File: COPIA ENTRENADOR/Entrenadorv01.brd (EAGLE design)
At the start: 116.1 x 96.2 mm, 67 parts, among them IC1 7805T, X1 MINI-USB_4P-85-32004-10X

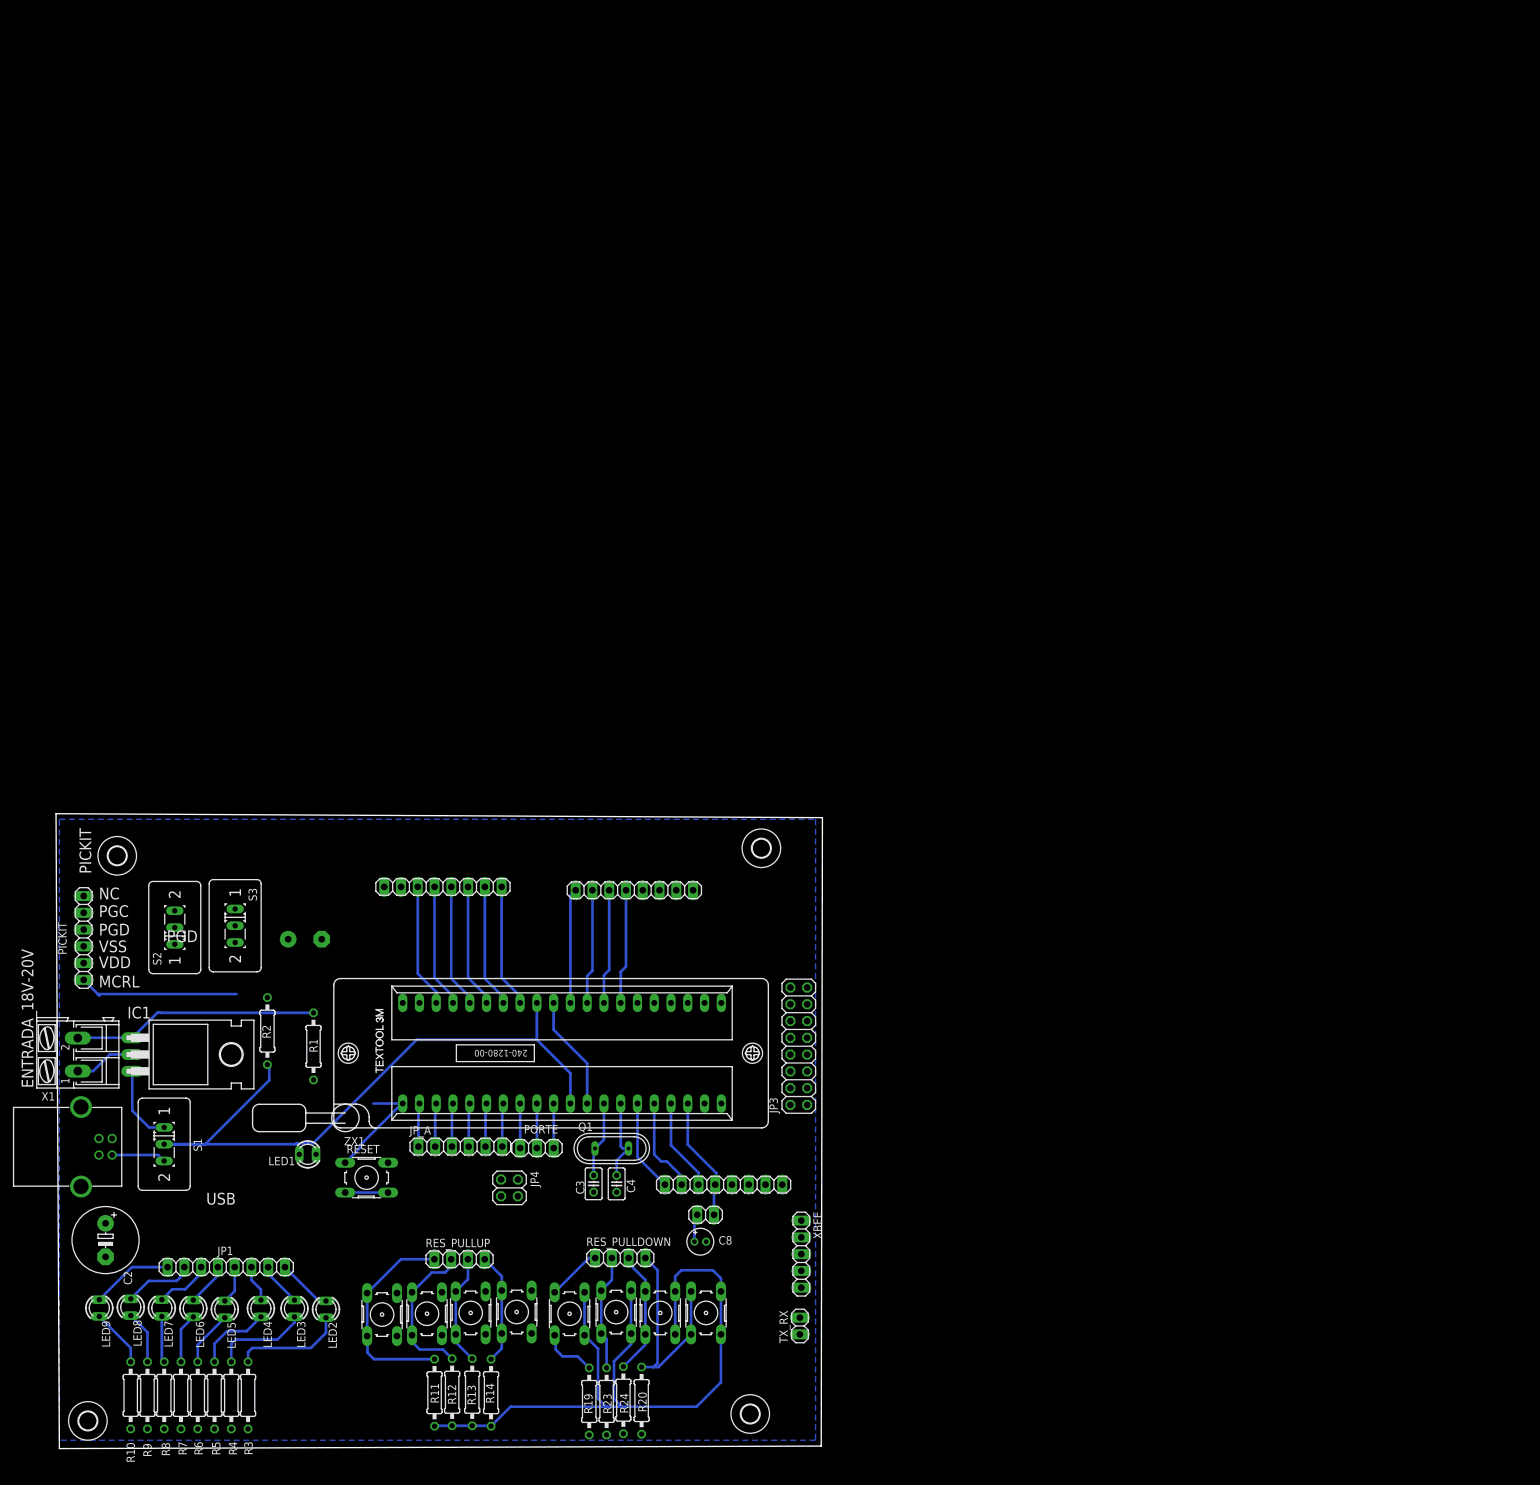
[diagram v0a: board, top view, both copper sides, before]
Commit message: se agrega diseño PCB
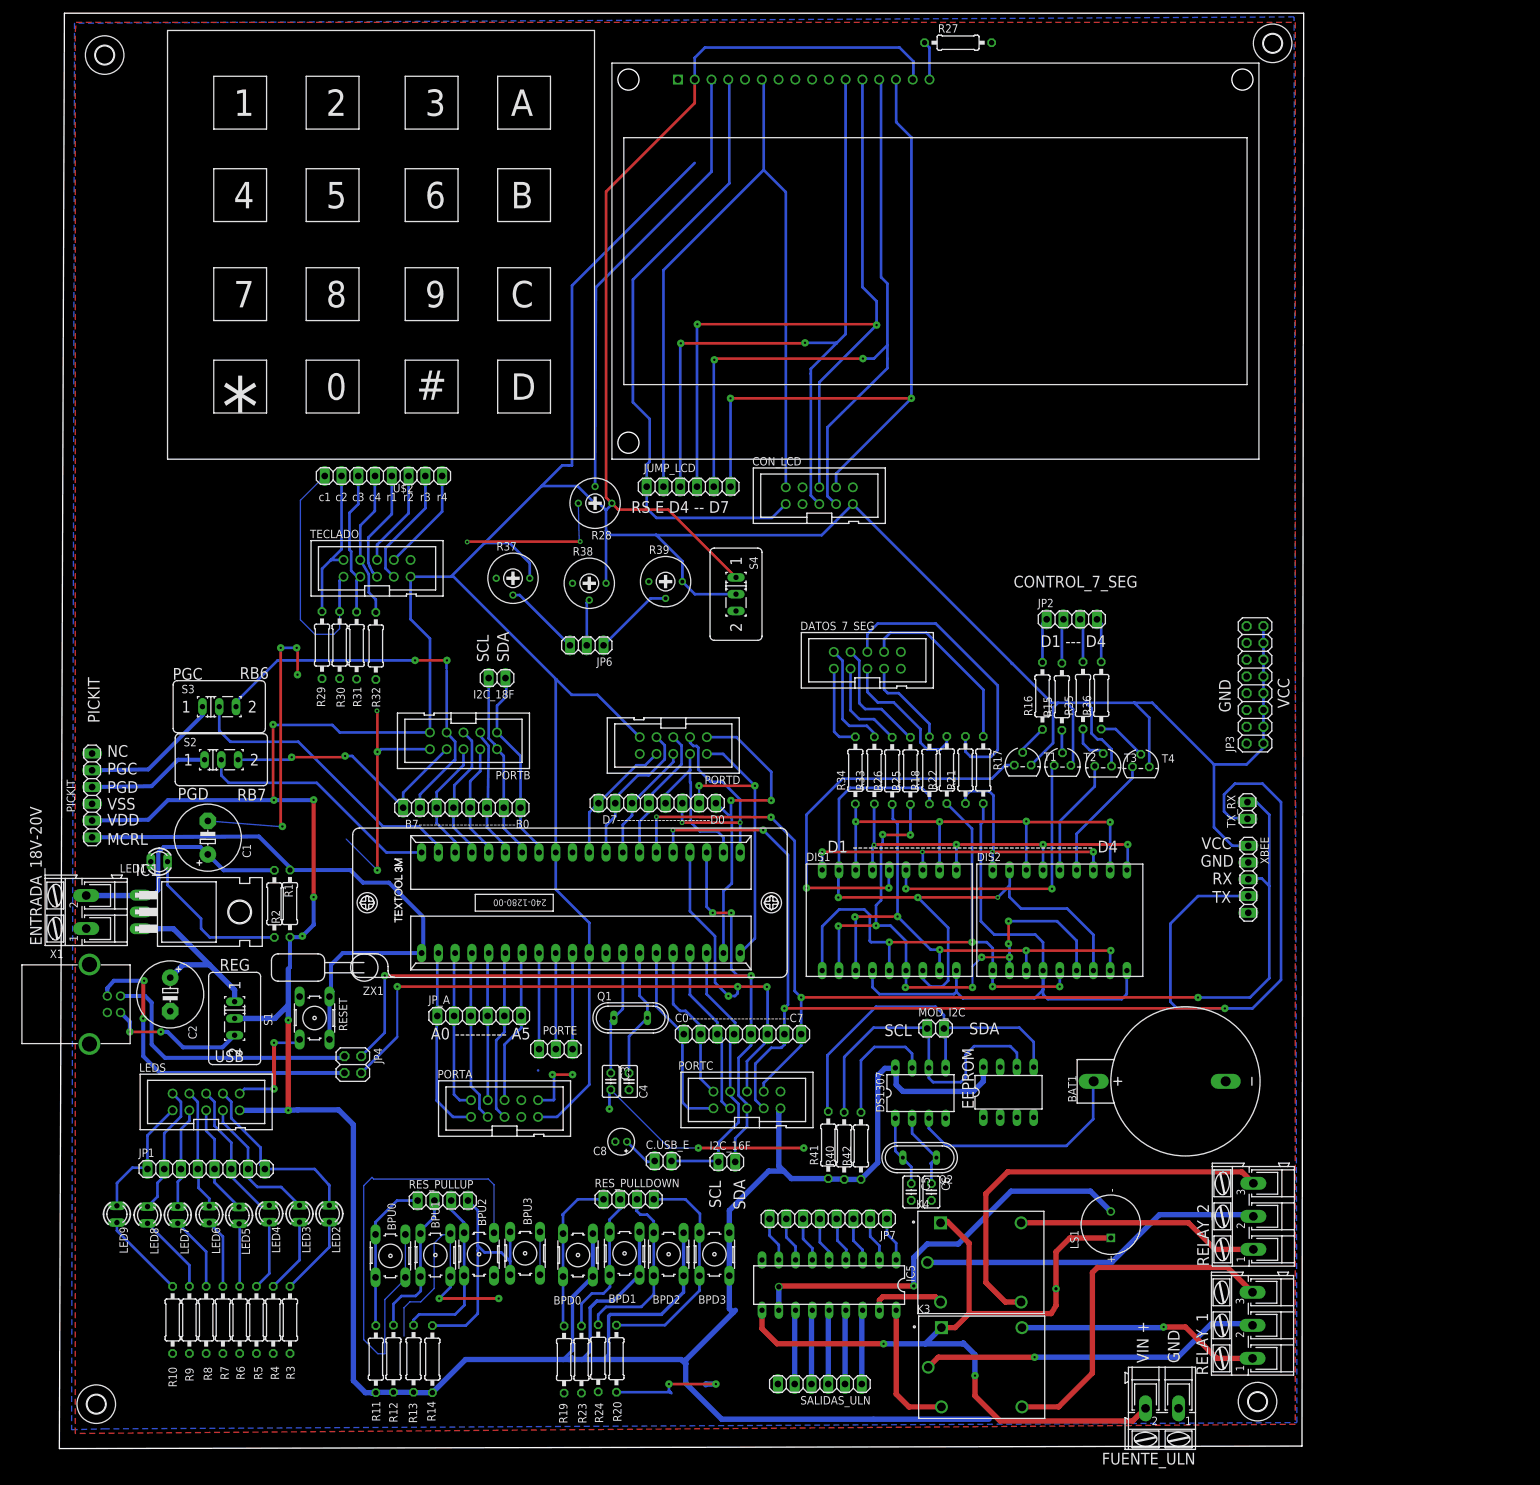
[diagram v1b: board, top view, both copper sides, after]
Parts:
- added BAT1: (no value), sn2032:SN2032
- added C5, C6: (no value), rcl:C025-025X050
- added CON_LCD, DATOS_7_SEG, LEDS, PORTA, PORTB, PORTC, PORTD, TECLADO: 2510-, con-3m:PAK100/2500-10
- added DIS1, DIS2: HD-K123, display-hp:HDSP-R
- added DS1307: DS1307, ds1307_pcf8583:DIL08
- added EEPROM: 24LC256P, microchip:DIL8
- added FUENTE_ULN: (no value), con-ptr500:AK300/2
- added I2C_16F, I2C_18F, MOD_I2C: (no value), pinhead:1X02
- added IC5: (no value), uln-udn:DIL18
- added JP2: (no value), pinhead:1X04
- added JP6: (no value), pinhead:1X03
- added JP7: (no value), pinhead:1X08
- added JUMP_LCD, SALIDAS_ULN: (no value), pinhead:1X06
- added K3, K4: SRD-05VDC-SL-C, SRD-05VDC-SL-C (1):RELAY_SRD-05VDC-SL-C
- added LS1: CST-951AP, CST-951AP:CUI_CST-951AP
- added Q2: (no value), special:QS
- added R15, R16, R29, R30, R31, R32, R35, R36: 10K, rcl:0207/10
- added R17, R18, R21, R22, R25, R26, R27, R33, R34: 330, rcl:0207/10
- added R28, R37, R38, R39: 5K, rcl:RTRIM3339P
- added R40, R41, R42: 10k, rcl:0207/10
- added RELAY_1, RELAY_2: (no value), con-ptr500:AK300/3
- added S4: (no value), switch:M251
- added T1, T2, T3, T4: 2N3904, transistor:TO92
- added U$1: LCD-HD4478020X4-3HOLES, HD44780LCD:LCD-20X4-3HOLES
- added U$2: (no value), keypad_4x4_raw:KEYPAD4X4
- moved U$6 144.4 mm to (183.8, 212.9)
- moved U$5 121.3 mm to (6.86, 211.1)
- moved TX_RX 103.4 mm to (180.0, 96.6)
- moved XBEE 88.4 mm to (180.1, 86.2)
- moved JP3 88.2 mm to (181.1, 115.7)
- moved U$4 76.9 mm to (181.5, 7.11)
- moved LED1 49.7 mm to (15.1, 88.9)
- moved C2 38.5 mm to (16.8, 68.8)
- moved S3 33.3 mm to (24.2, 112.4), turned to 0 degrees
- moved JP4 30.2 mm to (44.5, 58.2)
- moved S2 26.4 mm to (24.5, 104.3), turned to 0 degrees
- moved RESET 25.4 mm to (38.6, 65.2), turned to 270 degrees
- moved ZX1 23.0 mm to (79.0, 82.7)
- moved C0---------------------------C7 23.0 mm to (103.5, 62.8)
- moved R1 22.4 mm to (32.6, 82.5)
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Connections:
- new net A: DIS1.11, DIS1.16, DIS2.11, DIS2.16, R34.1
- new net B: DIS1.10, DIS1.15, DIS2.10, DIS2.15, R33.1
- new net C: DIS1.3, DIS1.8, DIS2.3, DIS2.8, R26.1
- new net D: DIS1.2, DIS1.6, DIS2.2, DIS2.6, R25.1
- new net E: DIS1.1, DIS1.5, DIS2.1, DIS2.5, R22.1
- new net F: DIS1.12, DIS1.18, DIS2.12, DIS2.18, R21.1
- new net G: DIS1.17, DIS1.7, DIS2.17, DIS2.7, R18.1
- new net N$10: JP6.2, R38.2
- new net N$100: FUENTE_ULN.2, IC5.10, K3.A1, K4.A1, LS1.P
- new net N$101: R28.1, S4.1, U$1.P$15, U$1.P$2
- new net N$12: JP6.3, R37.2
- new net N$13: R27.1, U$1.P$16
- new net N$14: JP6.1, R39.2
- new net N$15: IC5.1, JP7.1
- new net N$18: CON_LCD.8, JUMP_LCD.6, U$1.P$14
- new net N$19: CON_LCD.7, JUMP_LCD.5, U$1.P$13
- new net N$20: IC5.2, JP7.2
- new net N$21: CON_LCD.6, JUMP_LCD.4, U$1.P$12
- new net N$22: DS1307.6, EEPROM.6, MOD_I2C.1, R40.2
- new net N$23: CON_LCD.5, JUMP_LCD.3, U$1.P$11
- new net N$24: IC5.3, JP7.3
- new net N$25: CON_LCD.1, JUMP_LCD.1, U$1.P$4
- new net N$26: DIS1.4, DIS1.9, DIS2.4, DIS2.9, R17.2
- new net N$27: CON_LCD.2, JUMP_LCD.2, U$1.P$6
- new net N$28: R30.1, TECLADO.1, U$2.1
- new net N$29: R28.2, U$1.P$3
- new net N$30: R29.1, TECLADO.2, U$2.2
- new net N$31: R31.1, TECLADO.3, U$2.3
- new net N$32: R32.1, TECLADO.4, U$2.4
- new net N$33: TECLADO.5, U$2.5
- new net N$34: TECLADO.6, U$2.6
- new net N$35: TECLADO.7, U$2.7
- new net N$36: TECLADO.8, U$2.8
- new net N$37: DATOS_7_SEG.7, R18.2
- new net N$38: R16.1, T1.2
- new net N$40: R15.1, T2.2
- new net N$41: DIS1.13, T2.3
- new net N$42: DIS1.14, T1.3
- new net N$59: DATOS_7_SEG.6, R21.2
- new net N$60: JP2.1, R16.2
- new net N$61: JP2.2, R15.2
- new net N$62: DATOS_7_SEG.5, R22.2
- new net N$63: DATOS_7_SEG.4, R25.2
- new net N$64: DATOS_7_SEG.3, R26.2
- new net N$65: DATOS_7_SEG.2, R33.2
- new net N$66: DATOS_7_SEG.1, R34.2
- new net N$67: DATOS_7_SEG.8, R17.1
- new net N$68: R35.1, T3.2
- new net N$70: R36.1, T4.2
- new net N$71: JP2.4, R36.2
- new net N$72: JP2.3, R35.2
- new net N$73: DIS2.14, T3.3
- new net N$74: DIS2.13, T4.3
- new net N$75: IC5.4, JP7.4
- new net N$76: IC5.5, JP7.5
- new net N$77: BAT1.+, DS1307.3
- new net N$78: DS1307.7, R42.2
- new net N$79: IC5.6, JP7.6
- new net N$80: DS1307.5, EEPROM.5, MOD_I2C.2, R41.2
- new net N$81: C5.1, DS1307.1, Q2.2
- new net N$82: C6.1, DS1307.2, Q2.1
- new net N$83: IC5.7, JP7.7
- new net N$84: IC5.8, JP7.8
- new net N$85: IC5.11, LS1.M
- new net N$86: IC5.18, K3.A2
- new net N$87: K3.COM, RELAY_1.2
- new net N$88: IC5.14, SALIDAS_ULN.3
- new net N$89: IC5.17, K4.A2
- new net N$90: IC5.16, SALIDAS_ULN.1
- new net N$91: IC5.15, SALIDAS_ULN.2
- new net N$92: IC5.13, SALIDAS_ULN.4
- new net N$93: IC5.12, SALIDAS_ULN.5
- new net N$94: K3.NO, RELAY_1.3
- new net N$95: K3.NC, RELAY_1.1
- new net N$96: K4.NO, RELAY_2.3
- new net N$97: K4.COM, RELAY_2.2
- new net N$98: K4.NC, RELAY_2.1
- net AUX_B6: now also PORTB.7
- net AUX_B7: now also PORTB.8
- net GND: now also BAT1.-, C5.2, C6.2, CON_LCD.10, DS1307.4, EEPROM.1, EEPROM.2, EEPROM.3, EEPROM.4, EEPROM.7, FUENTE_ULN.1, IC5.9, LEDS.10, PORTA.10, PORTB.10, PORTC.10, PORTD.10, R27.2, R28.3, R29.2, R30.2, R31.2, R32.2, R37.1, R38.1, R39.1, SALIDAS_ULN.6, TECLADO.10, U$1.P$1, U$1.P$10, U$1.P$5, U$1.P$7, U$1.P$8, U$1.P$9
- net N$51: now also LEDS.1
- net N$52: now also LEDS.2
- net N$53: now also LEDS.3
- net N$54: now also LEDS.4
- net N$55: now also LEDS.5
- net N$56: now also LEDS.6
- net N$57: now also LEDS.7
- net N$58: now also LEDS.8
- net RA0: now also PORTA.1
- net RA1: now also PORTA.2
- net RA2: now also PORTA.3
- net RA3: now also PORTA.4
- net RA4: now also PORTA.5
- net RA5: now also PORTA.6
- net RB0: now also I2C_18F.1, PORTB.1
- net RB1: now also I2C_18F.2, PORTB.2
- net RB2: now also PORTB.3
- net RB3: now also PORTB.4
- net RB4: now also PORTB.5
- net RB5: now also PORTB.6
- net RC0: now also PORTC.1
- net RC1: now also PORTC.2
- net RC2: now also PORTC.3
- net RC3: now also I2C_16F.1, PORTC.4
- net RC4: now also I2C_16F.2, PORTC.5
- net RC5: now also PORTC.6
- net RC6: now also PORTC.7
- net RC7: now also PORTC.8
- net RD0: now also PORTD.1
- net RD1: now also PORTD.2
- net RD2: now also PORTD.3
- net RD3: now also PORTD.4
- net RD4: now also PORTD.5
- net RD5: now also PORTD.6
- net RD6: now also PORTD.7
- net RD7: now also PORTD.8
- net VCC: now also CON_LCD.9, DS1307.8, EEPROM.8, LEDS.9, PORTA.9, PORTB.9, PORTC.9, PORTD.9, R37.3, R38.3, R39.3, R40.1, R41.1, R42.1, S4.2, T1.1, T2.1, T3.1, T4.1, TECLADO.9
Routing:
- net VCC: track 221.3 -> 941.0 mm, vias 0 -> 7
- net GND: track 33.1 -> 308.8 mm, vias 0 -> 20
- net RC6: track 1.09 -> 220.8 mm, vias 0 -> 4
- net RC7: track 0.01 -> 173.2 mm, vias 0 -> 4
- net N$101: track 0.00 -> 134.6 mm
- net N$100: track 0.00 -> 127.4 mm, vias 0 -> 3
- net RC4: track 0.00 -> 123.9 mm, vias 0 -> 4
- net N$23: track 0.00 -> 119.0 mm, vias 0 -> 2
- net N$21: track 0.00 -> 118.1 mm, vias 0 -> 2
- net N$27: track 0.00 -> 117.9 mm
- net N$19: track 0.00 -> 115.9 mm, vias 0 -> 2
- net RC5: track 0.06 -> 115.7 mm, vias 0 -> 4
- net N$18: track 0.00 -> 108.2 mm, vias 0 -> 2
- net G: track 0.00 -> 103.0 mm, vias 0 -> 3
- net N$25: track 0.00 -> 94.9 mm
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- added copper zone on layer 1, net GND
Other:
- board size 116.1 x 96.2 mm -> 188.5 x 217.4 mm
- board text added: "A0 ---------- A5"
- board text added: "CONTROL_7_SEG"
- board text added: "D1 --- D4"
- board text added: "D1 ---------------------------------------------- D4"
- board text added: "GND"
- board text added: "RB6"
- board text added: "RB7"
- board text added: "REG"
- board text added: "RS E D4 -- D7"
- board text added: "RX"
- board text added: "SCL"
- board text added: "SDA"
- board text added: "TX"
- board text added: "VCC"
- board text added: "VIN +"
